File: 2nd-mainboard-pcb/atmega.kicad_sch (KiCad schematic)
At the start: 36 parts, among them J10 FAN2, J11 FAN4, J12 Fan_12/5V_Regelung, J3 T0, J4 T1, J5 T2, J6 T3, J8 FAN0, J9 FAN1, Q1 DTC143E, Q3 DTC143E, Q4 DTC143E, Q5 DTC143E, U1 ATmega328PB-A, U3 DRV8871DDA, Y1 ECS-160-18-4X-CKM

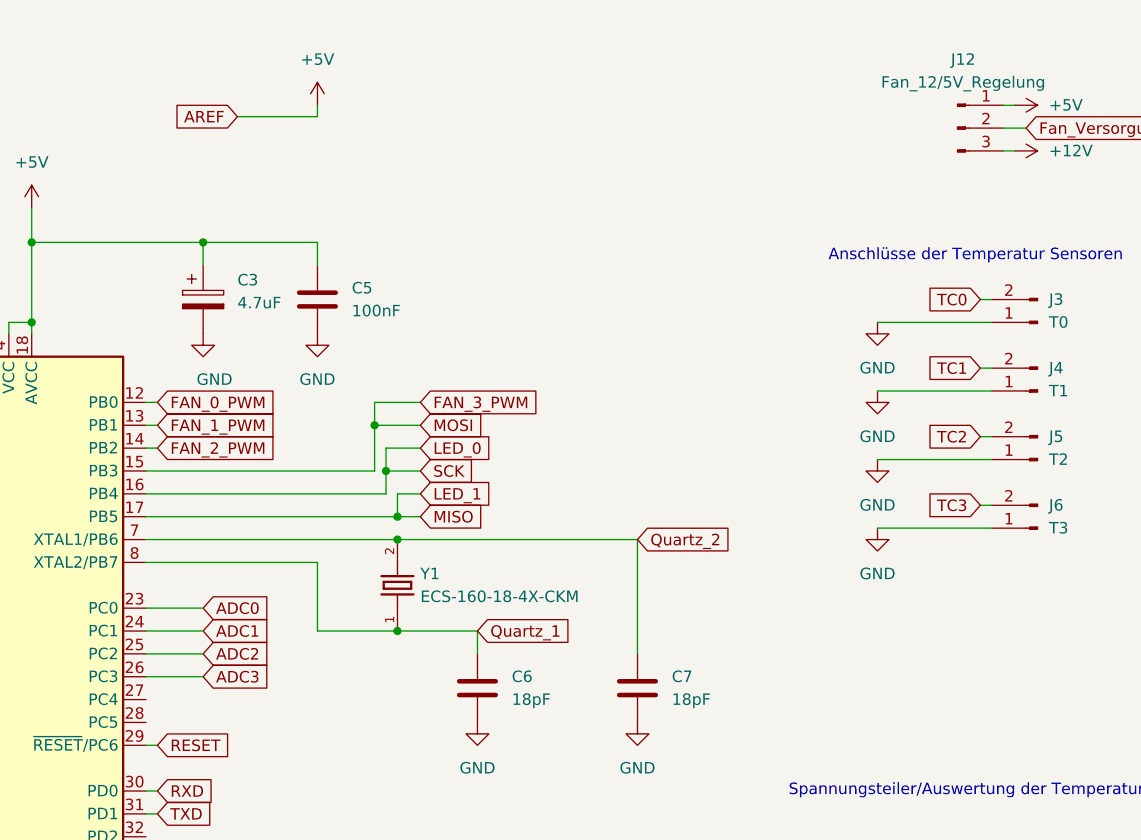
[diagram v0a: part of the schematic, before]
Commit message: added imported components, changed structure
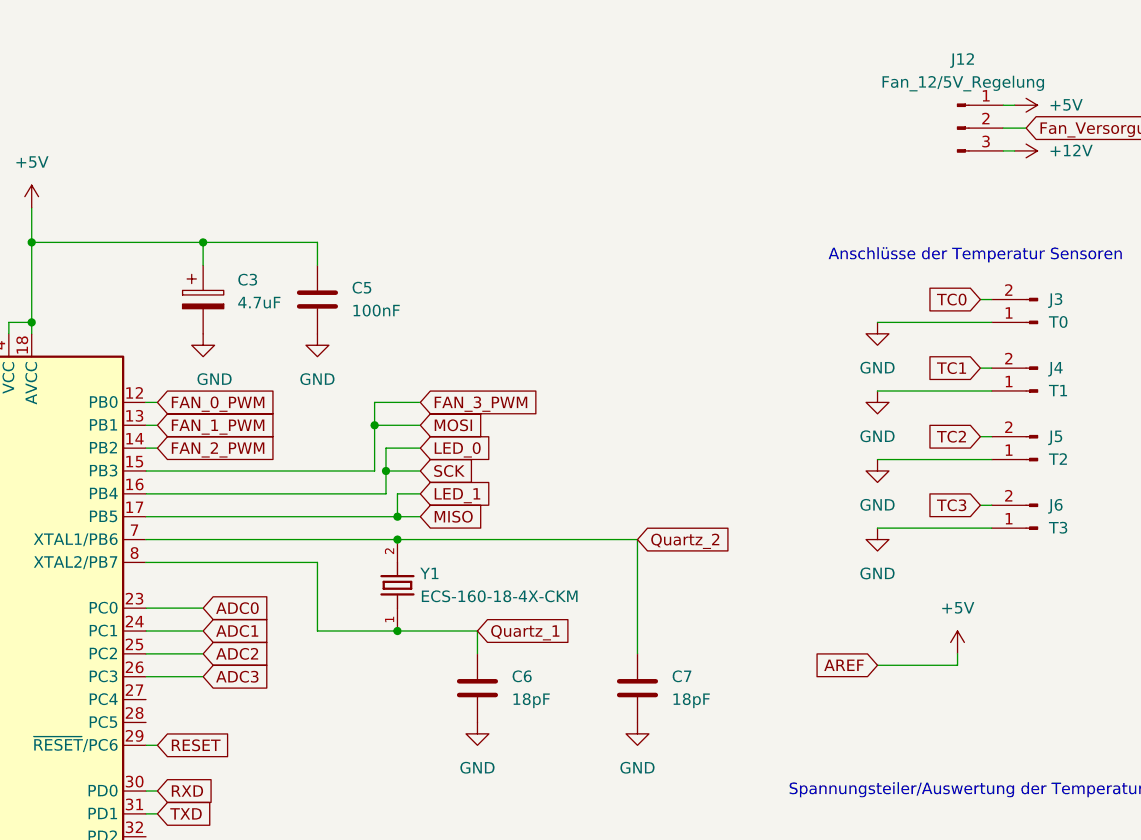
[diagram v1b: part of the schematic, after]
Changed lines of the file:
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@@
 	(wire
 		(pts
-			(xy 71.12 26.67) (xy 71.12 25.4)
-		)
-		(stroke
-			(width 0)
-			(type default)
-		)
-	)
-	(wire
-		(pts
-			(xy 62.23 26.67) (xy 71.12 26.67)
+			(xy 142.24 87.63) (xy 142.24 86.36)
+		)
+		(stroke
+			(width 0)
+			(type default)
+		)
+	)
+	(wire
+		(pts
+			(xy 133.35 87.63) (xy 142.24 87.63)
 		)
 		(stroke
@@
 	(global_label "AREF"
 		(shape input)
-		(at 62.23 26.67 180)
+		(at 133.35 87.63 180)
 		(fields_autoplaced yes)
 		(effects
@@
 		)
 		(property "Intersheetrefs" "${INTERSHEET_REFS}"
-			(at 54.6486 26.67 0)
+			(at 125.7686 87.63 0)
 			(effects
 				(font
@@
 	(symbol
 		(lib_id "power:+5V")
-		(at 71.12 25.4 0)
+		(at 142.24 86.36 0)
 		(unit 1)
 		(exclude_from_sim no)
@@
 		(fields_autoplaced yes)
 		(property "Reference" "#PWR024"
-			(at 71.12 29.21 0)
+			(at 142.24 90.17 0)
 			(effects
 				(font
@@
 		)
 		(property "Value" "+5V"
-			(at 71.12 20.32 0)
+			(at 142.24 81.28 0)
 			(effects
 				(font
@@
 		)
 		(property "Footprint" ""
-			(at 71.12 25.4 0)
+			(at 142.24 86.36 0)
 			(effects
 				(font
@@
 		)
 		(property "Datasheet" ""
-			(at 71.12 25.4 0)
+			(at 142.24 86.36 0)
 			(effects
 				(font
@@
 		)
 		(property "Description" "Power symbol creates a global label with name \"+5V\""
-			(at 71.12 25.4 0)
-			(effects
-				(font
+			(at 142.24 86.36 0)
+			(effects
+				(font

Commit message: verpolungsschutz und powerin
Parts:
- renumbered R7 to R6, R6 to R7
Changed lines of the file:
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@@
 		(dnp no)
 		(fields_autoplaced yes)
-		(property "Reference" "R7"
+		(property "Reference" "R6"
 			(at 163.83 115.5699 0)
 			(effects
@@
 			(project "2nd-mainboard-pcb"
 				(path "/6926a609-8b92-4b3a-88c8-3d023174b977/2814f85c-0b7e-4ab3-b3e5-bcf29424baab"
-					(reference "R7")
+					(reference "R6")
 					(unit 1)
 				)
@@
 		(dnp no)
 		(fields_autoplaced yes)
-		(property "Reference" "R6"
+		(property "Reference" "R7"
 			(at 134.62 115.5699 0)
 			(effects
@@
 			(project "2nd-mainboard-pcb"
 				(path "/6926a609-8b92-4b3a-88c8-3d023174b977/2814f85c-0b7e-4ab3-b3e5-bcf29424baab"
-					(reference "R6")
-					(unit 1)
-				)
+					(reference "R7")
+					(unit 1)
+				)

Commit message: finished stacked design, annotaded
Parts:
- removed D3, D4: YELLOW, LED_SMD:LED_0805_2012Metric, symbol Device:LED
- removed Q1, Q3, Q4, Q5: DTC143E, Package_TO_SOT_SMD:SOT-723, symbol Transistor_BJT:DTC143E
- removed R11, R8: 330, Resistor_SMD:R_0402_1005Metric, symbol Device:R
- removed U3: DRV8871DDA, Package_SO:Texas_HTSOP-8-1EP_3.9x4.9mm_P1.27mm_EP2.95x4.9mm_Mask2.4x3.1mm_ThermalVias, symbol Driver_Motor:DRV8871DDA
- added U10, U8: RJK0456DPB-00-J5, Imported_Component_Footprints:RJK0456DPB_00_J5, symbol Imported_Component_Symbols:RJK0456DPB-00-J5
- added U9: TPM16050-S6TR, Imported_Component_Footprints:TPM16050_S6TR, symbol Imported_Component_Symbols:TPM16050-S6TR
- J10: renamed from J9; value FAN1 -> FAN2
- J4: renamed from J10; value FAN2 -> FAN1; footprint Connector_PinHeader_2.54mm:PinHeader_1x02_P2.54mm_Horizontal -> Imported_Component_Footprints:CONN_S2B-XH-A-1LFSN_JST
- J5: renamed from J8; footprint Connector_PinHeader_2.54mm:PinHeader_1x02_P2.54mm_Horizontal -> Imported_Component_Footprints:CONN_S2B-XH-A-1LFSN_JST
- renumbered C3 to C19, C5 to C20, C6 to C21, C7 to C22, C9 to C23, C10 to C24, C11 to C25, C12 to C26, D5 to D4, D6 to D5, J12 to J3, J3 to J6, J4 to J7, J5 to J8, J6 to J9, R12 to R14, R13 to R15, R7 to R16, R6 to R17, R9 to R18, R10 to R19, U1 to U7
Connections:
- net DIR: now also U7.27 (PC4); no longer U7.1 (PD3)
- net FAN_2_PWM: now also U7.9 (PD5), U8.4 (G); no longer U7.14 (PB2)
- net FAN_3_PWM: now also U7.10 (PD6), U10.4 (G); no longer U7.15 (PB3)
- net Fan_Versorgung: now also U9.4 (VM); no longer J4.2 (Pin_2), J5.2 (Pin_2)
- net GND: now also U10.1 (S), U10.2, U10.3, U8.1 (S), U8.2, U8.3, U9.2 (GND)
- net STEP: now also U7.28 (PC5); no longer U7.2 (PD4)
- net at J11.1 (Pin_1): now also U10.5 (D)
- net at J5.1 (Pin_1): now also J4.1 (Pin_1), U9.1 (OUT2)
- net at J10.1 (Pin_1): now also U8.5 (D)
- net +5V renamed +5V_POW
- net +5V_POW: no longer R16.1, R17.1, R18.1, R19.1, U7.20 (AREF)
- net FAN_0_PWM: no longer names the net of U7.12 (PB0)
- net FAN_1_PWM renamed FAN_01_PWM_clockwise
- net FAN_01_PWM_clockwise: now also U9.6 (IN2)
- new net: J4.2 (Pin_2), J5.2 (Pin_2), U9.3 (OUT1)
- new net AREF: R16.1, R17.1, R18.1, R19.1, U7.20 (AREF)
- new net BLT_Servo: U7.1 (PD3)
- new net BLT_Switch: U7.2 (PD4)
- new net FAN_01_PWM_counterclockwise: U7.14 (PB2), U9.5 (IN1)
- new net SM_Servo: U7.15 (PB3)
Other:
- note added: "4 Fans sollen angeschlossen werden. Ein jeder soll mit 12 oder 5V betrieben werden können Zwei von Ihnen sollen auch softwaretechnisch ihre Richtung umkehren können, dabei sollen sie es gleichzeitig tun: FAN0 und FAN1 sollen entweder clock oder counterclockwise drehen"
- note added: "Die anderen Fans werden mit einem N-Channel Mos angetrieben. Dabei soll der Strom limitiert werden auf die jeweilige Leistugn der Fans"
- note added: "Hier Pow oder USB-C 5V verwenden?"
- note added: "Hier den Vorwiderstand von 26,9 Ohm auslassen, dass die Fans mit 12V gesteuert werden können"
- note added: "Je nachdem ob die Sensoren am Coldend/Hotend verbaut werden, werden auch die Widerstände anders dimensioniert um eine hohe Auflösung zu garantieren Natürlich wird dies im Schaltplan beachtet, sollte sich etwas ändern kann jedoch beim Aufbau auch einfach ein anderer Fan angelötet werden"
- note removed: "DRV8871 hier verbauen"
- moved on the sheet: C23, C24, C25, C26, D4, D5, J10, J3, J4, J5, J6, J7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

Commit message: alle bauteile hinzugefügt
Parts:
- removed J10: FAN2, Connector_PinHeader_2.54mm:PinHeader_1x02_P2.54mm_Horizontal, symbol Connector:Conn_01x02_Male
- removed J11: FAN4, Connector_PinHeader_2.54mm:PinHeader_1x02_P2.54mm_Horizontal, symbol Connector:Conn_01x02_Male
- removed J3: Fan_12/5V_Regelung, Connector_PinHeader_2.54mm:PinHeader_1x03_P2.54mm_Horizontal, symbol Connector:Conn_01x03_Pin
- removed J4: FAN1, Imported_Component_Footprints:CONN_S2B-XH-A-1LFSN_JST, symbol Connector:Conn_01x02_Male
- removed J5: FAN0, Imported_Component_Footprints:CONN_S2B-XH-A-1LFSN_JST, symbol Connector:Conn_01x02_Male
- removed J6: T0, Connector_PinHeader_2.54mm:PinHeader_1x02_P2.54mm_Horizontal, symbol Connector:Conn_01x02_Male
- removed J7: T1, Connector_PinHeader_2.54mm:PinHeader_1x02_P2.54mm_Horizontal, symbol Connector:Conn_01x02_Male
- removed J8: T2, Connector_PinHeader_2.54mm:PinHeader_1x02_P2.54mm_Horizontal, symbol Connector:Conn_01x02_Male
- removed J9: T3, Connector_PinHeader_2.54mm:PinHeader_1x02_P2.54mm_Horizontal, symbol Connector:Conn_01x02_Male
- added J10: T3, Imported_Component_Footprints:665102131822, symbol Imported_Component_Symbols:665102131822
- added J2: Fan_12/5V_Regelung, Imported_Component_Footprints:FTS_103_01_F_S, symbol Imported_Component_Symbols:FTS-103-01-F-S
- added J3: FAN0, Imported_Component_Footprints:CONN_S2B-XH-A-1LFSN_JST, symbol Imported_Component_Symbols:S2B-XH-A-1LFSN
- added J4: FAN1, Imported_Component_Footprints:CONN_S2B-XH-A-1LFSN_JST, symbol Imported_Component_Symbols:S2B-XH-A-1LFSN
- added J5: FAN2, Imported_Component_Footprints:CONN_S2B-XH-A-1LFSN_JST, symbol Imported_Component_Symbols:S2B-XH-A-1LFSN
- added J6: FAN3, Imported_Component_Footprints:CONN_S2B-XH-A-1LFSN_JST, symbol Imported_Component_Symbols:S2B-XH-A-1LFSN
- added J7, J8, J9: T2, Imported_Component_Footprints:665102131822, symbol Imported_Component_Symbols:665102131822
- C20: renamed from C19; footprint (none) -> Capacitor_SMD:C_0805_2012Metric_Pad1.18x1.45mm_HandSolder
- C21: renamed from C20; footprint (none) -> Capacitor_SMD:C_0402_1005Metric_Pad0.74x0.62mm_HandSolder
- C22: renamed from C21; footprint (none) -> Capacitor_SMD:C_0402_1005Metric_Pad0.74x0.62mm_HandSolder
- C23: renamed from C22; footprint (none) -> Capacitor_SMD:C_0402_1005Metric_Pad0.74x0.62mm_HandSolder
- C24: renamed from C23; footprint Capacitor_SMD:C_0402_1005Metric -> Capacitor_SMD:C_0402_1005Metric_Pad0.74x0.62mm_HandSolder
- C25: renamed from C24; footprint Capacitor_SMD:C_0402_1005Metric -> Capacitor_SMD:C_0402_1005Metric_Pad0.74x0.62mm_HandSolder
- C26: renamed from C25; footprint Capacitor_SMD:C_0402_1005Metric -> Capacitor_SMD:C_0402_1005Metric_Pad0.74x0.62mm_HandSolder
- C27: renamed from C26; footprint Capacitor_SMD:C_0402_1005Metric -> Capacitor_SMD:C_0402_1005Metric_Pad0.74x0.62mm_HandSolder
- Y1: footprint ECS-160-18-4X-CKM:XTAL_ECS-160-18-4X-CKM -> Imported_Component_Footprints:XTAL_ECS-160-18-4X-CKM
- renumbered D4 to D3, D5 to D4, R16 to R12, R17 to R13, R18 to R14, R19 to R15, R14 to R16, R15 to R17, U7 to U10, U9 to U7, U10 to U9
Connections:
- net +12V: now also J2.3
- net +5V_POW: now also J2.1
- net ADC0: now also J7.2
- net ADC1: now also J8.2
- net ADC2: now also J9.2
- net ADC3: now also J10.2
- net Fan_Versorgung: now also J2.2, J5.1, J6.1
- net GND: now also J10.1, J7.1, J8.1, J9.1
- net LED_0: now also U10.3 (PE0); no longer U10.16 (PB4)
- net LED_1: now also U10.6 (PE1); no longer U10.17 (PB5)
- net at U7.1 (OUT2): now also J3.2, J4.2
- net at U7.3 (OUT1): now also J3.1, J4.1
- net at U9.5 (D): now also J6.2
- net at U8.5 (D): now also J5.2
- net SM_Servo renamed MOSI
- new net MISO: U10.16 (PB4)
- new net SCK: U10.17 (PB5)
- no-connect marks 0 -> 5

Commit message: new arrangement pcb
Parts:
- added D6, D7: YELLOW, LED_SMD:LED_0805_2012Metric, symbol Device:LED
- added R24, R25: 330, Resistor_SMD:R_0402_1005Metric, symbol Device:R
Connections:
- net DIR: now also U10.32 (PD2); no longer U10.27 (PC4)
- net GND: now also R24.2, R25.2
- net STEP: now also U10.11 (PD7); no longer U10.28 (PC5)
- net LED_2: now reaches U10.19 (PE2)
- net LED_2: now also D6.2 (A)
- net LED_3: now reaches U10.22 (PE3)
- net LED_3: now also D7.2 (A)
- new net: D7.1 (K), R25.1
- new net: D6.1 (K), R24.1
- new net SMD_TEMP_0: U10.27 (PC4)
- new net SMD_TEMP_1: U10.28 (PC5)
- no-connect marks 5 -> 1
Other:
- note added: "Fans-Modul"

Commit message: Fan-PCB-Beginning
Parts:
- removed C24, C25, C26, C27: 0.1µF, Capacitor_SMD:C_0402_1005Metric_Pad0.74x0.62mm_HandSolder, symbol Device:C
- removed J10: T3, Imported_Component_Footprints:665102131822, symbol Imported_Component_Symbols:665102131822
- removed J7, J8, J9: T2, Imported_Component_Footprints:665102131822, symbol Imported_Component_Symbols:665102131822
- removed R12, R13, R14, R15: 4k7, Resistor_SMD:R_0402_1005Metric, symbol Device:R
- renumbered C20 to C19, C21 to C20, C22 to C21, C23 to C22, D7 to D3, D3 to D4, D4 to D5, R25 to R12, R16 to R13, R17 to R14, R24 to R15
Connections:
- net SMD_TEMP_0 renamed SDA
- net SMD_TEMP_1 renamed SCL
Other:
- added sheet Temperatur Messungen (temperatur_messungen.kicad_sch)
- note added: "Je nachdem ob es sich mit dem Platz auf der pLatine ausgeht, können diese ausgeführt werden, oder nicht."
- note removed: "Anschlüsse der Temperatur Sensoren"
- note removed: "Fans-Modul"
- note removed: "Hier Pow oder USB-C 5V verwenden?"
- note removed: "Je nachdem ob die Sensoren am Coldend/Hotend verbaut werden, werden auch die Widerstände anders dimensioniert um eine hohe Auflösung zu garantieren Natürlich wird dies im Schaltplan beachtet, sollte sich etwas ändern kann jedoch beim Aufbau auch einfach ein anderer Fan angelötet werden"
- note removed: "Spannungsteiler/Auswertung der Temperatur Sensoren"
- moved on the sheet: D3, D4, D5, D6, R12, R13, R14, R15

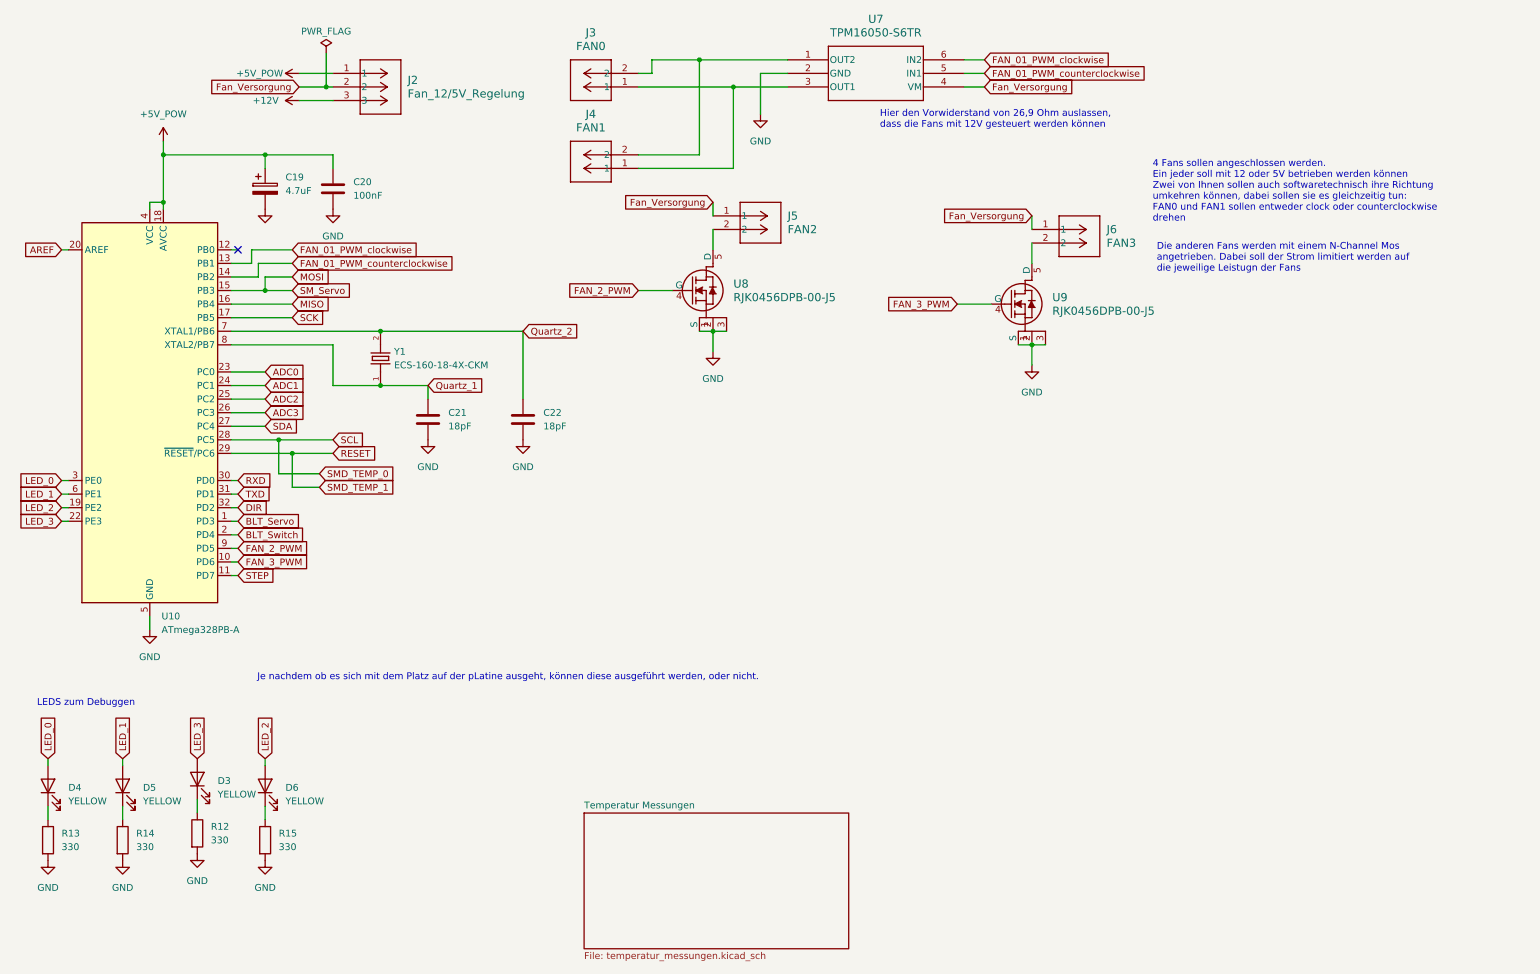
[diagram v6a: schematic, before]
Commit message: updated a bit of the track widths, removed comments in schematic
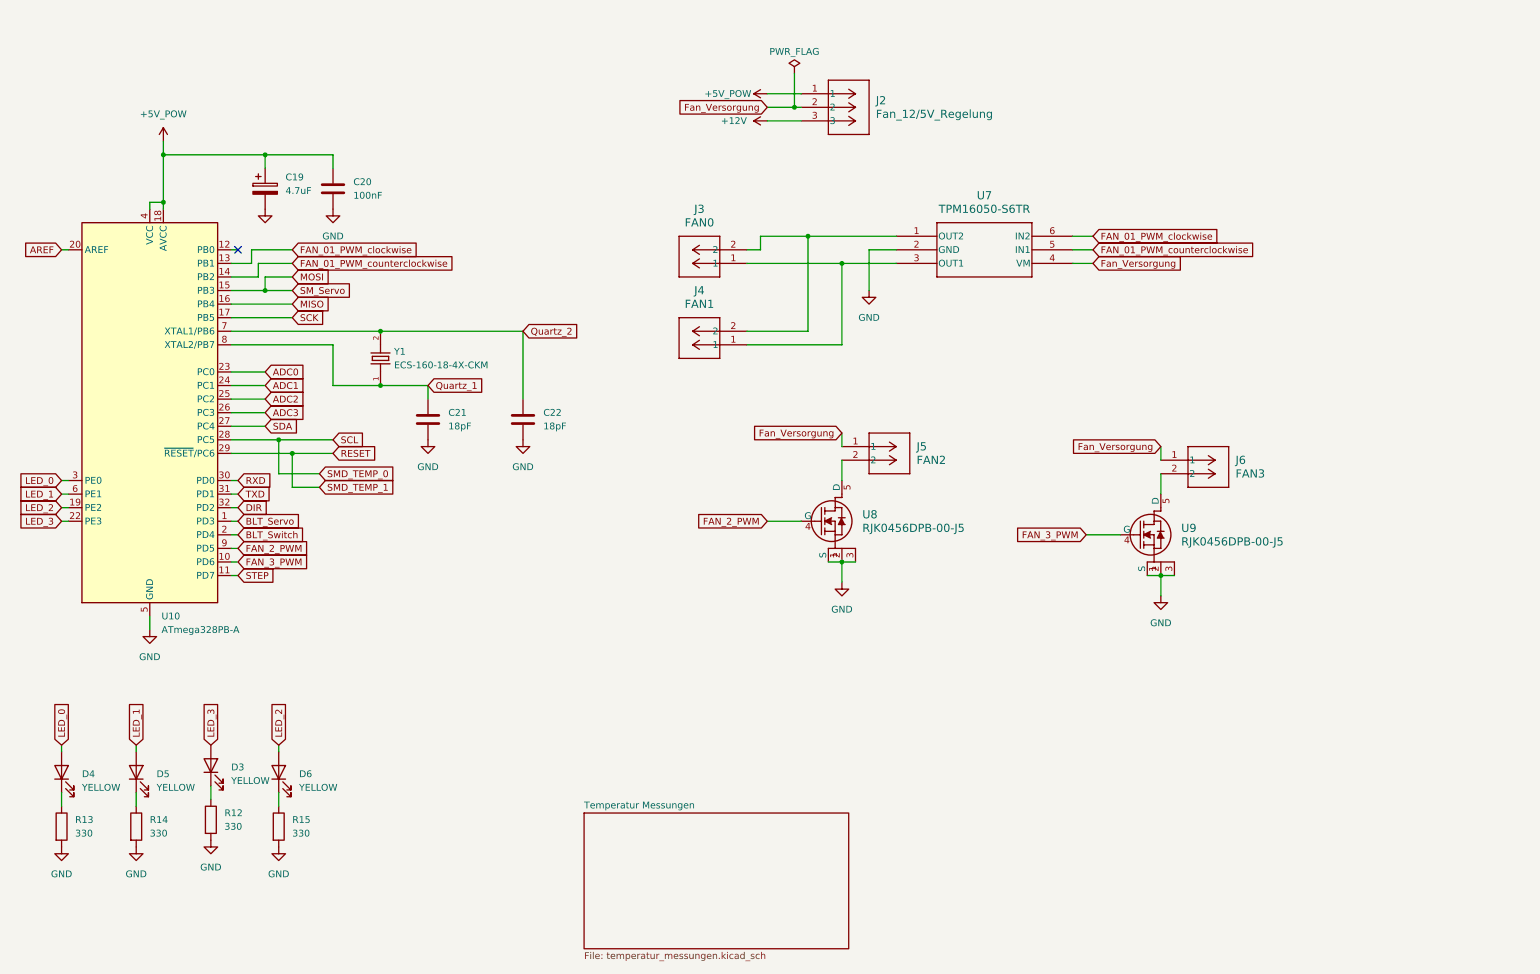
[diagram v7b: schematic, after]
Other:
- note removed: "4 Fans sollen angeschlossen werden. Ein jeder soll mit 12 oder 5V betrieben werden können Zwei von Ihnen sollen auch softwaretechnisch ihre Richtung umkehren können, dabei sollen sie es gleichzeitig tun: FAN0 und FAN1 sollen entweder clock oder counterclockwise drehen"
- note removed: "Die anderen Fans werden mit einem N-Channel Mos angetrieben. Dabei soll der Strom limitiert werden auf die jeweilige Leistugn der Fans"
- note removed: "Hier den Vorwiderstand von 26,9 Ohm auslassen, dass die Fans mit 12V gesteuert werden können"
- note removed: "Je nachdem ob es sich mit dem Platz auf der pLatine ausgeht, können diese ausgeführt werden, oder nicht."
- note removed: "LEDS zum Debuggen"
- moved on the sheet: D3, D4, D5, D6, J2, J3, J4, J5, J6, R12, R13, R14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
